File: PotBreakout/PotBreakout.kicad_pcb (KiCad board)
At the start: 2 copper layers, 24.1 x 30.5 mm, 2 parts, among them J1 Conn_02x07_Odd_Even, U1 PDB183GTR21

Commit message: Finalized pot breakout board
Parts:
- moved J1 0.63 mm to (160.7, 95.2)
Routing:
- net WIPE1: track 19.0 -> 16.0 mm
- net WIPE2: track 15.2 -> 13.1 mm
- net DPDT2: track 18.5 -> 16.9 mm
- net DPDT4: track 15.3 -> 14.2 mm
- net DPDT1: track 15.6 -> 14.6 mm
- net DPDT3: track 14.7 -> 13.8 mm
- net GANG21: track 21.3 -> 20.6 mm
- net DPDT6: track 11.5 -> 10.9 mm
- net GND: track 10.9 -> 10.3 mm
- net DPDT5: track 10.7 -> 10.0 mm
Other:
- board size 24.1 x 30.5 mm -> 26.2 x 30.2 mm
- board text added: "1"
- board text added: "2"
- board text added: "3"
- board text added: "4"
- board text added: "5"
- board text added: "6"
- board text added: "G11"
- board text added: "G13"
- board text added: "G21"
- board text added: "G23"
- board text added: "GND"
- board text added: "W1"
- board text added: "W2"

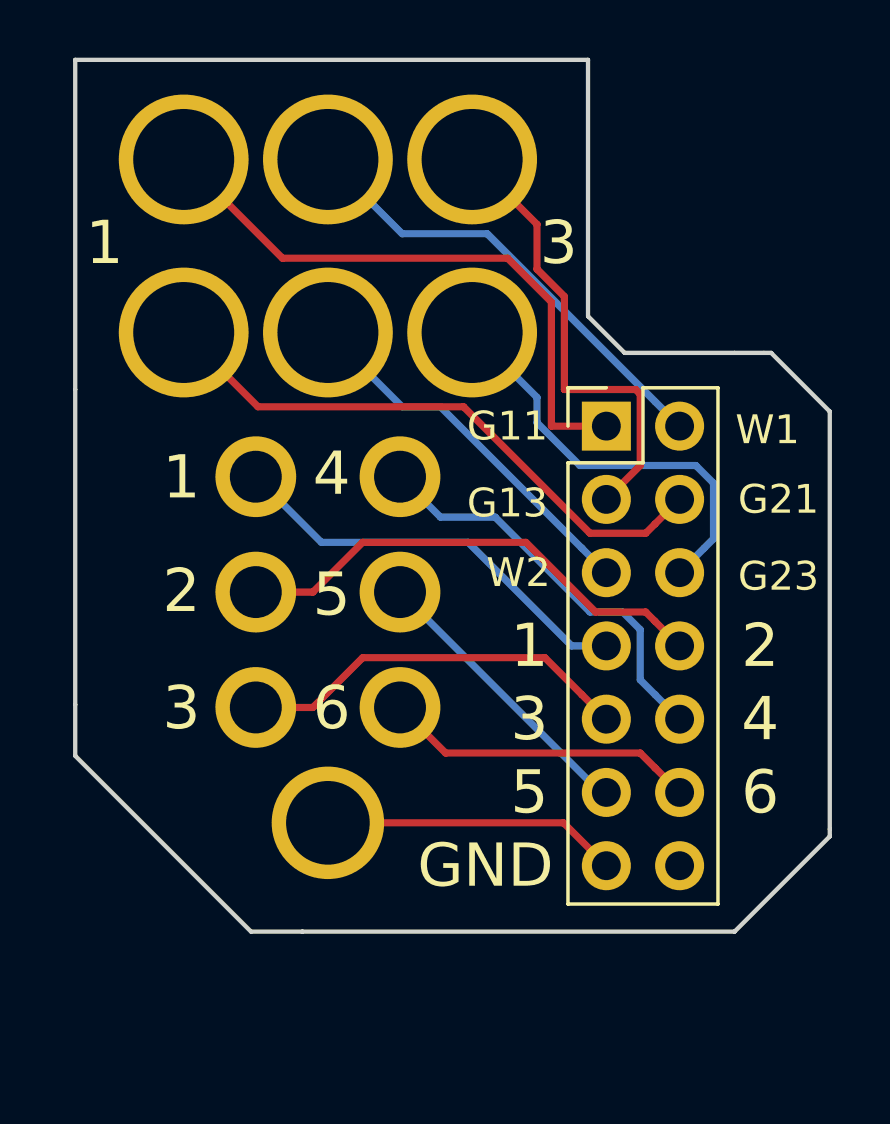
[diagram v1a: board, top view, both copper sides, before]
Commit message: altered pot breakout
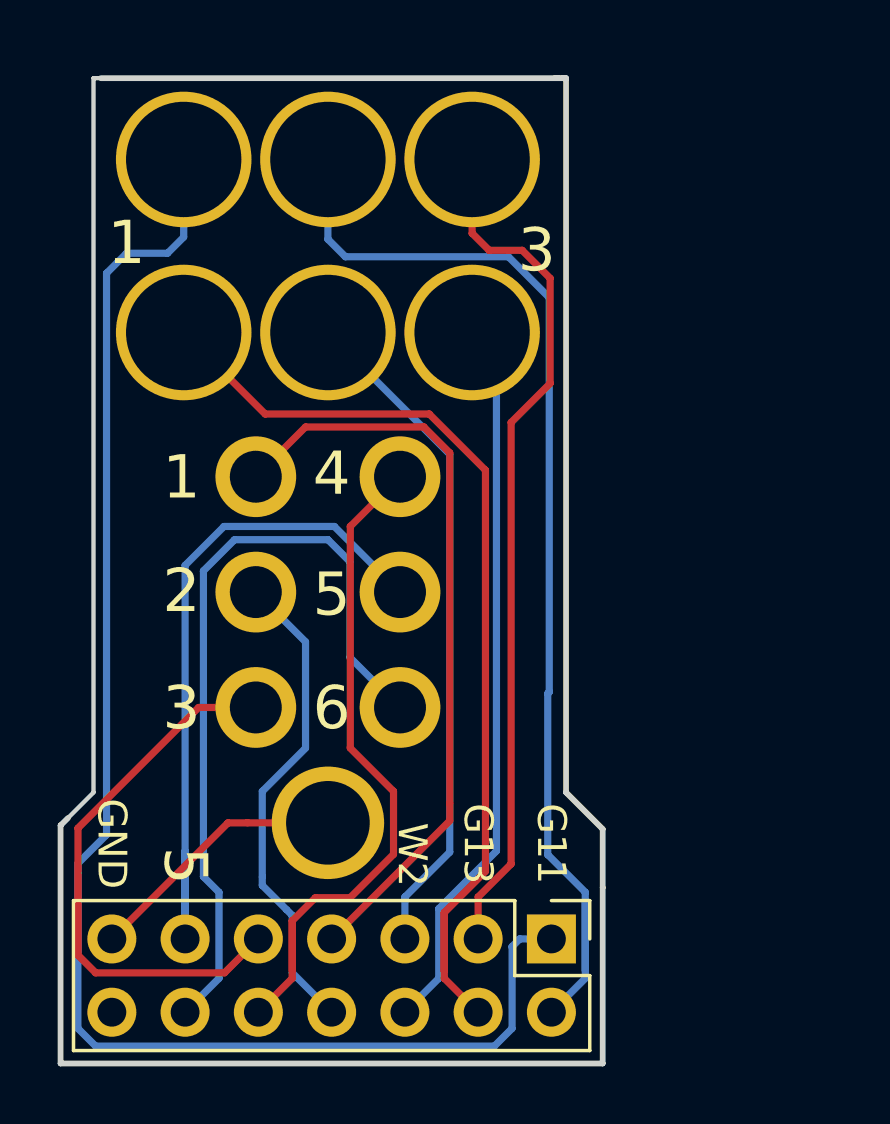
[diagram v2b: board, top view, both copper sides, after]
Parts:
- moved J1 17.9 mm to (158.8, 113.0), turned to 270 degrees
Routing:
- net GANG11: track 21.6 -> 52.4 mm
- net WIPE1: track 16.0 -> 39.5 mm
- net DPDT6: track 10.9 -> 27.6 mm
- net DPDT5: track 10.0 -> 24.7 mm
- net GANG21: track 20.6 -> 34.3 mm
- net GANG13: track 16.1 -> 29.6 mm
- net DPDT1: track 14.6 -> 26.4 mm
- net GANG23: track 14.6 -> 25.2 mm
- net DPDT4: track 14.2 -> 24.3 mm
- net WIPE2: track 13.1 -> 23.2 mm
- net DPDT3: track 13.8 -> 19.3 mm
- net GND: track 10.3 -> 9.16 mm
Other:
- board size 26.2 x 30.2 mm -> 18.8 x 34.2 mm
- board text removed: "G21"
- board text removed: "G23"
- board text removed: "W1"
